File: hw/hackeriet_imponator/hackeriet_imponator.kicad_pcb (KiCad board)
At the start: 2 copper layers, 257.6 x 124.6 mm, 16 parts, among them J1 AVR-ISP-6, J2 Battery connector, U1 ATmega328PB-A

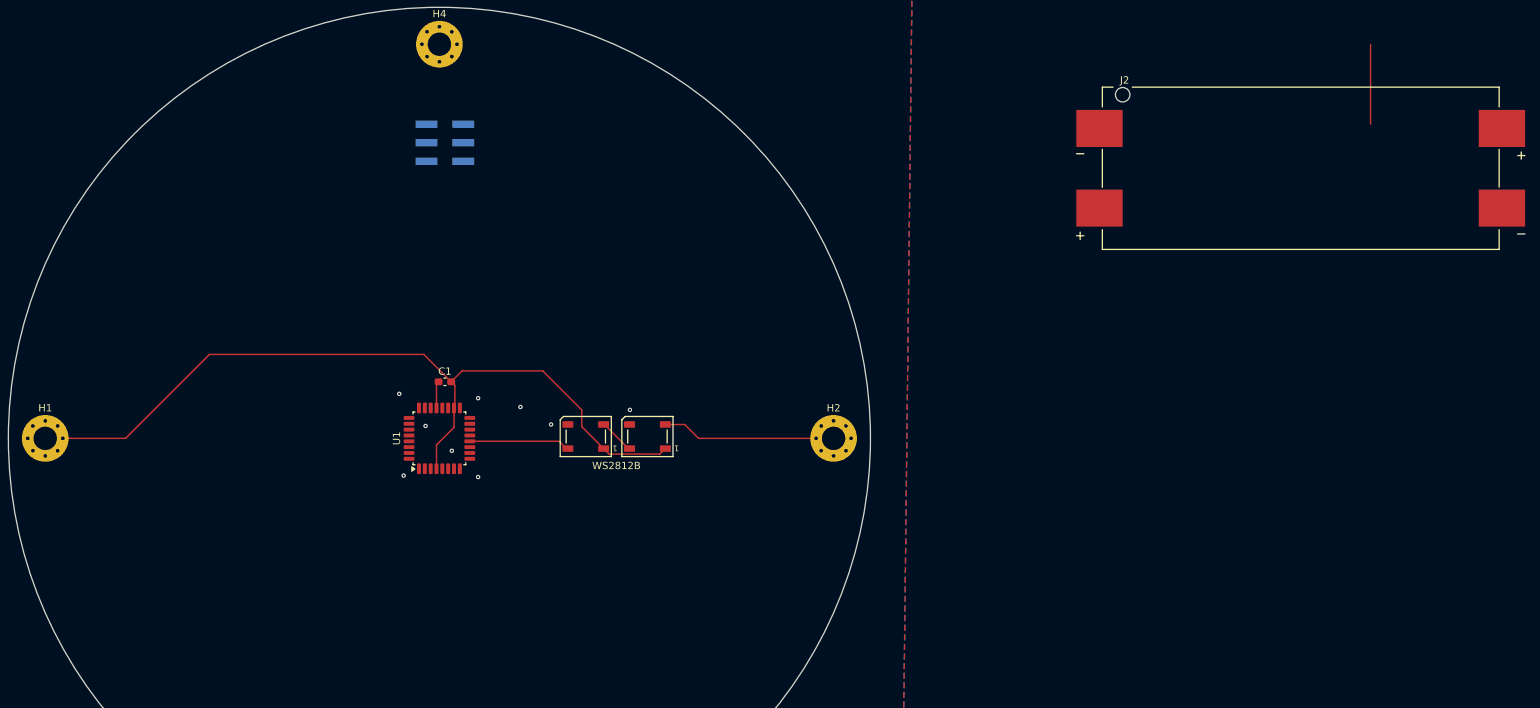
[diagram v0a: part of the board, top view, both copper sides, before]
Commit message: Added Batttery holders. Some general routing
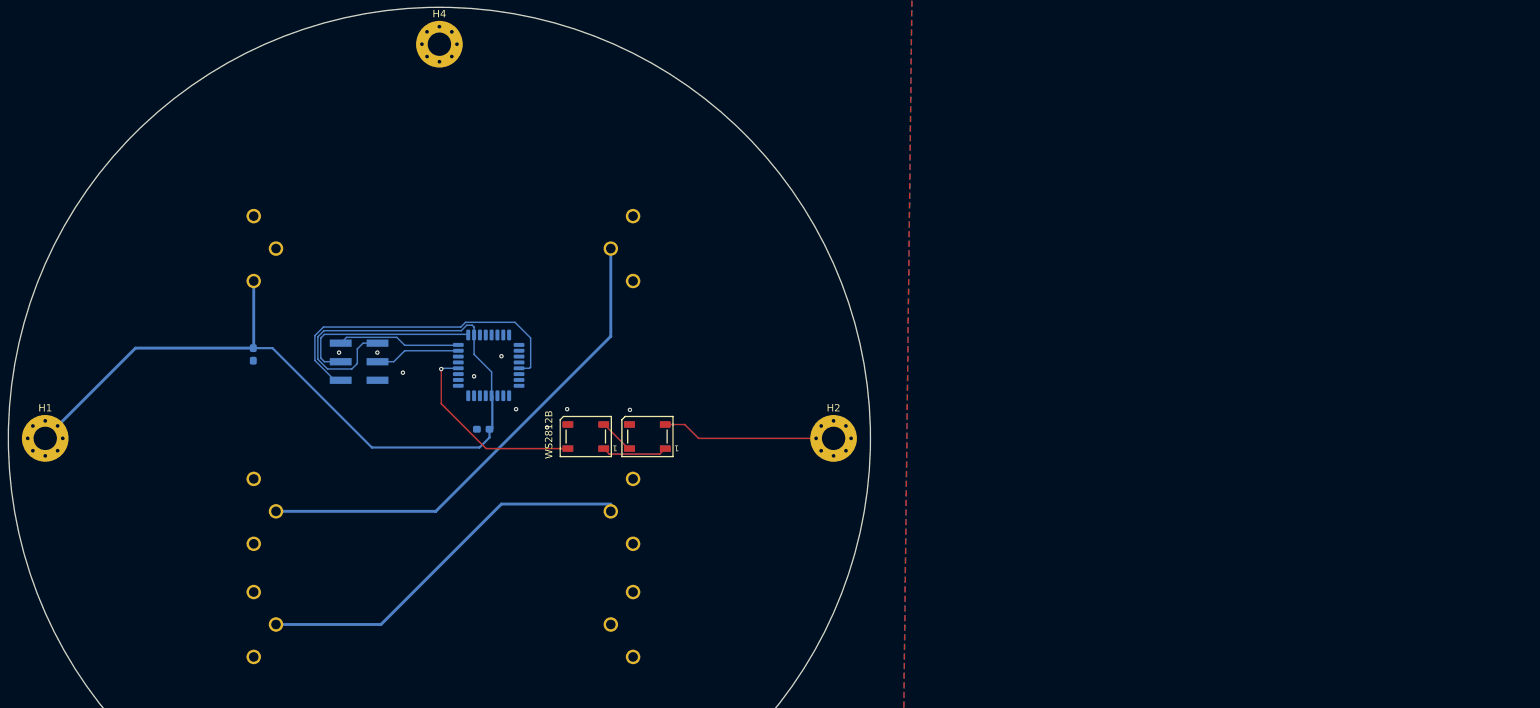
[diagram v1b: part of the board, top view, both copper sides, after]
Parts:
- added C2: 22uF, Capacitor_SMD:C_0603_1608Metric_Pad1.08x0.95mm_HandSolder, B.Cu at (154.0, 73.0)
- added J3: AAA -, imponator_footprint_lib:BAT_591, B.Cu at (203.0, 58.5)
- added J4: AAA +, imponator_footprint_lib:BAT_597, B.Cu at (157.1, 94.5)
- added J5: AAA -, imponator_footprint_lib:BAT_591, B.Cu at (203.0, 94.5)
- added J6: AAA +, imponator_footprint_lib:BAT_597, B.Cu at (157.1, 110.0)
- added J7: AAA -, imponator_footprint_lib:BAT_591, B.Cu at (203.0, 110.0)
- added REF**: AAA Battery Example, imponator_footprint_lib:AAA Battery Example, B.Cu at (179.5, 103.7)
- added REF**: AAA Battery Example, imponator_footprint_lib:AAA Battery Example, B.Cu at (179.5, 119.2)
- added REF**: AAA Battery Example, imponator_footprint_lib:AAA Battery Example, B.Cu at (179.5, 67.7)
- C1, U1: moved to B.Cu
- J2: value Battery connector -> AAA +; footprint imponator_footprint_lib:BAT_1022 -> imponator_footprint_lib:BAT_597; moved to B.Cu
- moved J2 140.8 mm to (157.1, 58.5), turned to -90 degrees
- moved J1 32.2 mm to (168.5, 74.0)
- moved U1 12.1 mm to (186.2, 74.5)
- moved C1 8.36 mm to (185.5, 83.2)
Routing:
- net Net-(J3-Pin_1): track 0.00 -> 67.8 mm
- net Net-(J5-Pin_1): track 0.00 -> 52.7 mm
- net Net-(J1-~{RST}): track 0.00 -> 44.9 mm
- net +3.3V: track 215.6 -> 247.7 mm
- net Net-(J1-SCK): track 0.00 -> 26.1 mm
- net Net-(J1-MISO): track 0.00 -> 16.9 mm
- net Net-(D1-DIN): track 13.9 -> 27.0 mm, vias 0 -> 1
- net Net-(J1-MOSI): track 0.00 -> 11.7 mm
- net Net-(J2-Pin_2): track 10.9 -> 0.00 mm
- net GND: track 3.77 -> 0.00 mm, vias 7 -> 9
- net (no net): vias 2 -> 0

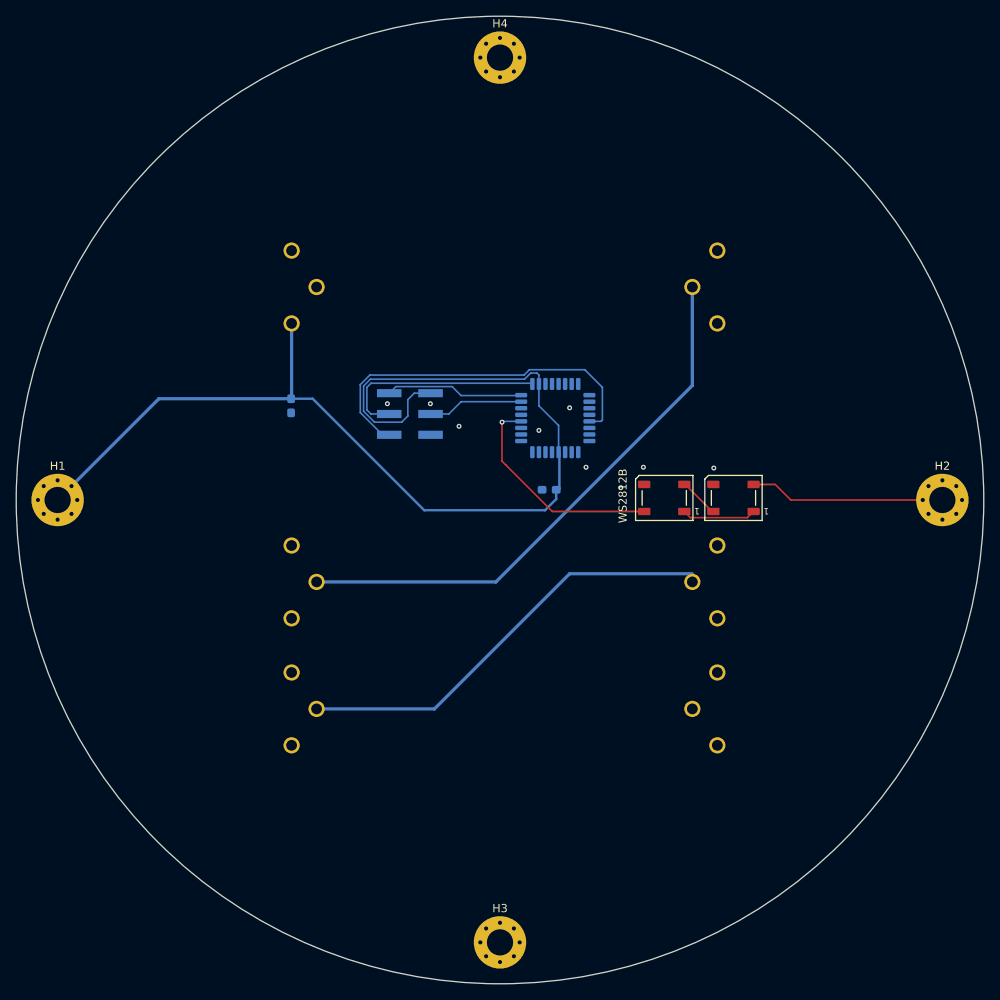
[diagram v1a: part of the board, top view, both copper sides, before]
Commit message: Imported SVG of logo directly to line stuff up better. Also better silkscreen.
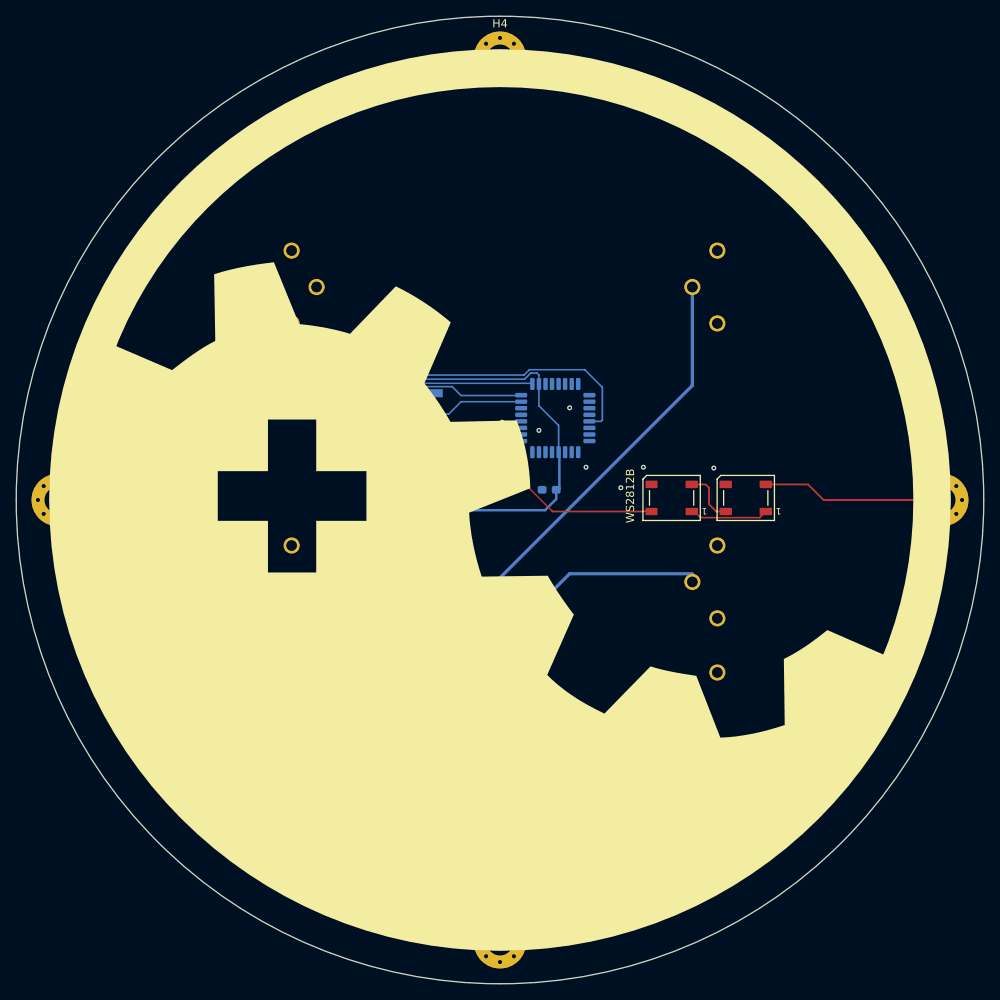
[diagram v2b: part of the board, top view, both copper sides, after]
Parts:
- moved D2 1.50 mm to (209.5, 84.2)
- moved D1 0.90 mm to (200.4, 84.2)
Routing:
- net Net-(D1-DOUT): track 4.92 -> 6.69 mm
- net Net-(D2-DOUT): track 23.8 -> 22.3 mm
- net Net-(D1-DIN): track 27.0 -> 27.9 mm
- net +3.3V: track 247.7 -> 248.3 mm

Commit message: Added cutout
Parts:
- moved D5 44.1 mm to (99.8, 148.7)
- moved D6 44.1 mm to (34.1, 119.4)
- moved H10 44.1 mm to (137.8, 96.9)
- moved H11 44.1 mm to (83.8, 150.9)
- moved H12 44.1 mm to (83.8, 42.9)
- moved H9 44.1 mm to (29.8, 96.9)
- moved C1 39.1 mm to (223.8, 91.4)
- moved C2 39.1 mm to (192.2, 81.2)
- moved D1 39.1 mm to (238.7, 92.4)
- moved D2 39.1 mm to (247.8, 92.4)
- moved H1 39.1 mm to (163.8, 92.7)
- moved H2 39.1 mm to (271.8, 92.7)
- moved H3 39.1 mm to (217.8, 146.7)
- moved H4 39.1 mm to (217.8, 38.6)
- moved J1 39.1 mm to (206.8, 82.2)
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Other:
- board size 257.6 x 124.6 mm -> 252.1 x 122.4 mm

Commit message: Major change. Resized PCB. Changed CPU. Added USB. Added headers. Added another layer for batteries
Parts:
- removed D6: WS2812B, LED_SMD:LED_WS2812B_PLCC4_5.0x5.0mm_P3.2mm
- removed the J7 at (241.2, 118.2)
- removed the REF** at (217.8, 127.3)
- removed the REF** at (217.8, 75.8)
- added C3: 22uF, Capacitor_SMD:C_0603_1608Metric_Pad1.08x0.95mm_HandSolder, B.Cu at (209.8, 63.5)
- added D3: WS2812B, LED_SMD:LED_WS2812B_PLCC4_5.0x5.0mm_P3.2mm, F.Cu at (157.2, 90.5)
- added D4: WS2812B, LED_SMD:LED_WS2812B_PLCC4_5.0x5.0mm_P3.2mm, B.Cu at (51.7, 121.7)
- added H5: MountingHole_Pad, MountingHole:MountingHole_2.5mm_Pad_TopBottom, F.Cu at (36.1, 63.7)
- added H6: MountingHole_Pad, MountingHole:MountingHole_2.5mm_Pad_TopBottom, F.Cu at (67.2, 117.6)
- added H7: MountingHole_Pad, MountingHole:MountingHole_2.5mm_Pad_TopBottom, F.Cu at (24.7, 106.2)
- added H8: MountingHole_Pad, MountingHole:MountingHole_2.5mm_Pad_TopBottom, F.Cu at (78.6, 75.1)
- added J11: AAA -, imponator_footprint_lib:BAT_591, B.Cu at (234.1, 108.1)
- added J4: Shitty Add On, Connector_PinHeader_2.54mm:PinHeader_2x02_P2.54mm_Horizontal, F.Cu at (162.6, 96.4)
- added J5: Unused pins, Connector_PinSocket_2.54mm:PinSocket_1x05_P2.54mm_Vertical_SMD_Pin1Left, B.Cu at (123.6, 119.1)
- added J8: AAA +, imponator_footprint_lib:BAT_597, B.Cu at (189.8, 96.2)
- added J9: AAA -, imponator_footprint_lib:BAT_591, B.Cu at (240.3, 84.9)
- added R1: 5.1K, Resistor_SMD:R_0603_1608Metric_Pad0.98x0.95mm_HandSolder, B.Cu at (138.2, 66.7)
- added R2: 5.1K, Resistor_SMD:R_0603_1608Metric_Pad0.98x0.95mm_HandSolder, B.Cu at (129.1, 66.7)
- added R3: 10k, Resistor_SMD:R_0603_1608Metric_Pad0.98x0.95mm_HandSolder, B.Cu at (139.5, 90.6)
- added R4: 4.7K, Resistor_SMD:R_0603_1608Metric_Pad0.98x0.95mm_HandSolder, B.Cu at (139.8, 101.3)
- added R5: 4.7K, Resistor_SMD:R_0603_1608Metric_Pad0.98x0.95mm_HandSolder, B.Cu at (143.4, 100.5)
- added REF**: Stap hole, imponator_footprint_lib:strap_hole, F.Cu at (143.7, 60.7)
- added REF**: Stap hole, imponator_footprint_lib:strap_hole, F.Cu at (123.7, 60.7)
- added REF**: AAA Battery Example, imponator_footprint_lib:AAA Battery Example, B.Cu at (217.5, 78.8)
- added REF**: AAA Battery Example, imponator_footprint_lib:AAA Battery Example, B.Cu at (211.3, 102.0)
- added U2: MCP2221AxSL, Package_SO:SOIC-14_3.9x8.7mm_P1.27mm, B.Cu at (134.0, 76.7)
- C2: value 22uF -> 1uF
- D1: value WS2812B -> Rx LED; footprint LED_SMD:LED_WS2812B_PLCC4_5.0x5.0mm_P3.2mm -> LED_SMD:LED_0603_1608Metric_Pad1.05x0.95mm_HandSolder; moved to B.Cu
- H1: value MountingHole_Pad -> M2, BATT; footprint MountingHole:MountingHole_3.2mm_M3_Pad_Via -> MountingHole:MountingHole_2.5mm_Pad_TopBottom
- H10, H11, H12, H9: footprint MountingHole:MountingHole_3.2mm_M3_Pad_Via -> MountingHole:MountingHole_2.5mm_Pad_TopBottom
- H2: value MountingHole_Pad -> M2 DOUT; footprint MountingHole:MountingHole_3.2mm_M3_Pad_Via -> MountingHole:MountingHole_2.5mm_Pad_TopBottom
- H3, H4: value MountingHole_Pad -> M2 GND; footprint MountingHole:MountingHole_3.2mm_M3_Pad_Via -> MountingHole:MountingHole_2.5mm_Pad_TopBottom
- J1: value AVR-ISP-6 -> USB4085-GF-A; footprint Connector_PinSocket_2.54mm:PinSocket_2x03_P2.54mm_Vertical_SMD -> Connector_USB:USB_C_Receptacle_GCT_USB4085; moved to F.Cu
- J2: value AAA + -> UPDI Programming; footprint imponator_footprint_lib:BAT_597 -> Connector_PinHeader_2.54mm:PinHeader_1x03_P2.54mm_Horizontal; moved to F.Cu
- J3: value AAA - -> External Battery Connector; footprint imponator_footprint_lib:BAT_591 -> Connector_PinHeader_2.54mm:PinHeader_1x02_P2.54mm_Vertical; moved to F.Cu
- U1: value ATmega328PB-A -> ATtiny804-SS; footprint Package_QFP:TQFP-32_7x7mm_P0.8mm -> Package_SO:SOIC-14_3.9x8.7mm_P1.27mm
- moved H9 173.6 mm to (200.1, 63.7), turned to -15 degrees
- moved H12 162.1 mm to (242.6, 75.1), turned to -15 degrees
- moved H2 125.0 mm to (149.2, 117.6), turned to -15 degrees
- moved H3 118.2 mm to (106.7, 106.2), turned to -15 degrees
- moved H11 114.1 mm to (188.7, 106.2), turned to -15 degrees
- moved C1 101.8 mm to (122.0, 95.6), turned to 90 degrees
- moved D2 99.1 mm to (148.7, 90.3)
- moved D1 99.0 mm to (143.0, 66.9), turned to -90 degrees
- moved D5 98.1 mm to (20.7, 90.7), turned to -90 degrees
- moved U1 96.5 mm to (128.9, 95.5), turned to -90 degrees
- moved H10 95.7 mm to (231.2, 117.6), turned to -15 degrees
- moved J3 89.0 mm to (152.3, 65.6), turned to 50 degrees
- moved J1 73.0 mm to (136.6, 61.8)
- moved H4 67.8 mm to (160.6, 75.1), turned to -15 degrees
- moved C2 67.1 mm to (125.2, 77.1), turned to -90 degrees
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- renumbered J5 to J10, J4 to J7
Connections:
- C1 pad 2: +3.3V -> BATT
- C2 pad 1: GND -> Net-(U2-VUSB)
- C2 pad 2: +3.3V -> GND
- D1 pad 1: +3.3V -> GND
- D1 pad 2: Net-(D1-DOUT) -> Net-(D1-A)
- D2 pad 1: +3.3V -> BATT
- D2 pad 4: Net-(D1-DOUT) -> WS2812B LED RGB Control
- D5 pad 1: +3.3V -> BATT
- D5 pad 2: Net-(D5-DOUT) -> unconnected-(D5-DOUT-Pad2)
- D5 pad 4: Net-(D5-DIN) -> Net-(D4-DOUT)
- H1 pad 1: +3.3V -> BATT
- H10 pad 1: Net-(D5-DIN) -> unconnected-(H10-Pad1)
- H2 pad 1: Net-(D2-DOUT) -> RGB DOUT, to top PCB
- H9 pad 1: +3.3V -> BATT
- J10 pad 1: Net-(J5-Pin_1) -> Net-(J10-Pin_1)
- J2 pad 1: +3.3V -> BATT
- J3 pad 1: Net-(J3-Pin_1) -> GND
- J6 pad 1: Net-(J5-Pin_1) -> BATT
- J7 pad 1: Net-(J3-Pin_1) -> Net-(J7-Pin_1)
- U1 pad 1: unconnected-(U1-PD3-Pad1) -> BATT
- U1 pad 10: unconnected-(U1-PD6-Pad10) -> Net-(J2-Pin_2)
- U1 pad 11: unconnected-(U1-PD7-Pad11) -> WS2812B LED RGB Control
- U1 pad 12: Net-(D1-DIN) -> MCP2221 _RST
- U1 pad 13: unconnected-(U1-PB1-Pad13) -> PA3
- U1 pad 14: unconnected-(U1-PB2-Pad14) -> GND
- U1 pad 2: unconnected-(U1-PD4-Pad2) -> PA4
- U1 pad 3: unconnected-(U1-PE0-Pad3) -> PA5
- U1 pad 4: +3.3V -> PA6
- U1 pad 5: GND -> PA7
- U1 pad 6: unconnected-(U1-PE1-Pad6) -> Attiny UART RX
- U1 pad 7: unconnected-(U1-XTAL1/PB6-Pad7) -> Attiny UART TX
- U1 pad 8: unconnected-(U1-XTAL2/PB7-Pad8) -> SDA
- U1 pad 9: unconnected-(U1-PD5-Pad9) -> SCL
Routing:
- net BATT: track 0.00 -> 454.1 mm, vias 0 -> 7
- net +3.3V: track 248.3 -> 0.00 mm
- net Net-(D5-DOUT): track 73.6 -> 0.00 mm
- net Net-(J10-Pin_1): track 0.00 -> 71.0 mm
- net Net-(J7-Pin_1): track 0.00 -> 69.6 mm
- net Net-(J3-Pin_1): track 67.8 -> 0.00 mm
- net Net-(D5-DIN): track 67.1 -> 0.00 mm
- net Net-(J5-Pin_1): track 52.7 -> 0.00 mm
- net Net-(D4-DOUT): track 0.00 -> 48.1 mm
- net PA3: track 0.00 -> 47.3 mm
- net RGB DOUT, to top PCB: track 0.00 -> 45.0 mm, vias 0 -> 1
- net Net-(J1-~{RST}): track 44.9 -> 0.00 mm
- net PA7: track 0.00 -> 42.5 mm
- net SCL: track 0.00 -> 42.5 mm
- net PA5: track 0.00 -> 41.7 mm
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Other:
- board size 252.1 x 122.4 mm -> 234 x 70 mm
- board text added: "BATT"
- board text added: "DATA"
- board text added: "External Battery Connector"
- board text added: "GND"
- board text added: "Shitty Add-on"

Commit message: Added paneling with mouse bites
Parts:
- added mouse-bite-3mm-slot: VAL**, imponator_footprint_lib:mouse-bite-3mm-slot, F.Cu at (88.8, 109.5)
- added mouse-bite-3mm-slot: VAL**, imponator_footprint_lib:mouse-bite-3mm-slot, F.Cu at (106.9, 78.1)
- added mouse-bite-3mm-slot: VAL**, imponator_footprint_lib:mouse-bite-3mm-slot, F.Cu at (125.1, 109.5)
- moved C3 119.9 mm to (101.1, 114.2)
- moved H10 119.9 mm to (122.5, 168.3)
- moved H11 119.9 mm to (80.0, 156.9)
- moved H9 119.9 mm to (91.4, 114.4)
- moved J6 119.9 mm to (87.3, 123.8)
- moved J7 119.9 mm to (84.8, 135.5)
- moved J8 119.9 mm to (81.1, 146.9)
- moved REF** 119.9 mm to (106.3, 141.3)
- moved H12 119.9 mm to (133.9, 125.8)
- moved J10 119.9 mm to (129.1, 147.4)
- moved J11 119.9 mm to (125.4, 158.8)
- moved J9 119.9 mm to (131.6, 135.6)
- moved REF** 119.9 mm to (108.8, 129.5)
- moved REF** 119.9 mm to (102.6, 152.7)
- moved D4 22.6 mm to (70.5, 109.1)
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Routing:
- net BATT: track 454.1 -> 453.2 mm
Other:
- board size 234 x 70 mm -> 142.7 x 133 mm

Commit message: Added final touches. This version will be ordered
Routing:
- net BATT: track 453.2 -> 453.9 mm
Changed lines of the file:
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@@
 			(at 0 -3.45 195)
 			(layer "B.SilkS")
+			(hide yes)
 			(effects
 				(font
@@
 			(at 3.936401 -2.210485 195)
 			(layer "B.SilkS")
+			(hide yes)
 			(effects
 				(font
@@
 			(at 0 -3.45 195)
 			(layer "B.SilkS")
+			(hide yes)
 			(effects
 				(font
@@
 			(at 0 -3.45 195)
 			(layer "B.SilkS")
+			(hide yes)
 			(effects
 				(font
@@
 			(at 3.067068 -1.977548 195)
 			(layer "B.SilkS")
+			(hide yes)
 			(effects
 				(font
@@
 		)
 		(fp_line
-			(start 4.15 2.109999)
+			(start 4.15 2.109998)
 			(end 10.150001 2.11)
 			(stroke
@@
 			(at 0 -3.45 195)
 			(layer "B.SilkS")
+			(hide yes)
 			(effects
 				(font
@@
 	)
 	(segment
+		(start 154.44775 88.4365)
+		(end 153.02375 87.0125)
+		(width 0.2)
+		(layer "B.Cu")
+		(net 3)
+	)
+	(segment
 		(start 149.12375 77.125)
 		(end 149.43625 77.4375)
@@
 	)
 	(segment
-		(start 170.102223 87.659027)
-		(end 169.455696 87.0125)
-		(width 0.2)
-		(layer "B.Cu")
-		(net 3)
-	)
-	(segment
 		(start 93.232559 100.1375)
 		(end 99.732559 93.6375)
@@
 	)
 	(segment
+		(start 169.32475 88.4365)
+		(end 154.44775 88.4365)
+		(width 0.2)
+		(layer "B.Cu")
+		(net 3)
+	)
+	(segment
 		(start 85.487332 118.683888)
 		(end 97.364169 118.683888)
@@
 	)
 	(segment
+		(start 170.102223 87.659027)
+		(end 169.32475 88.4365)
+		(width 0.2)
+		(layer "B.Cu")
+		(net 3)
+	)
+	(segment
 		(start 155.073807 77.4375)
 		(end 155.374807 77.1365)
@@
 		(width 0.2)
 		(layer "B.Cu")
-		(net 3)
-	)
-	(segment
-		(start 169.455696 87.0125)
-		(end 153.02375 87.0125)
-		(width 0.2)
-		(layer "B.Cu")
